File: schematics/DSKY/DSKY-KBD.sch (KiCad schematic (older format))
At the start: 64 parts, among them SW1 SW_Push, SW10 SW_Push, SW11 SW_Push, SW12 SW_Push, SW13 SW_Push, SW14 SW_Push, SW15 SW_Push, SW16 SW_Push, SW17 SW_Push, SW18 SW_Push, SW19 SW_Push, SW2 SW_Push, SW3 SW_Push, SW4 SW_Push, SW5 SW_Push, SW6 SW_Push, SW7 SW_Push, SW8 SW_Push, SW9 SW_Push, U1 74LS273, U10 74LS20, U11 74LS20, U12 74LS20, U13 74LS02, U14 74LS27, U15 74LS27, U16 74LS74, U18 74LS00, U19 74LS04, U2 74LS244, U3 LM555, U36 74LS00, U4 74LS04, U47 74LS126, U5 74LS04, U6 74LS00, U7 74LS08, U8 74LS10, U9 74LS20

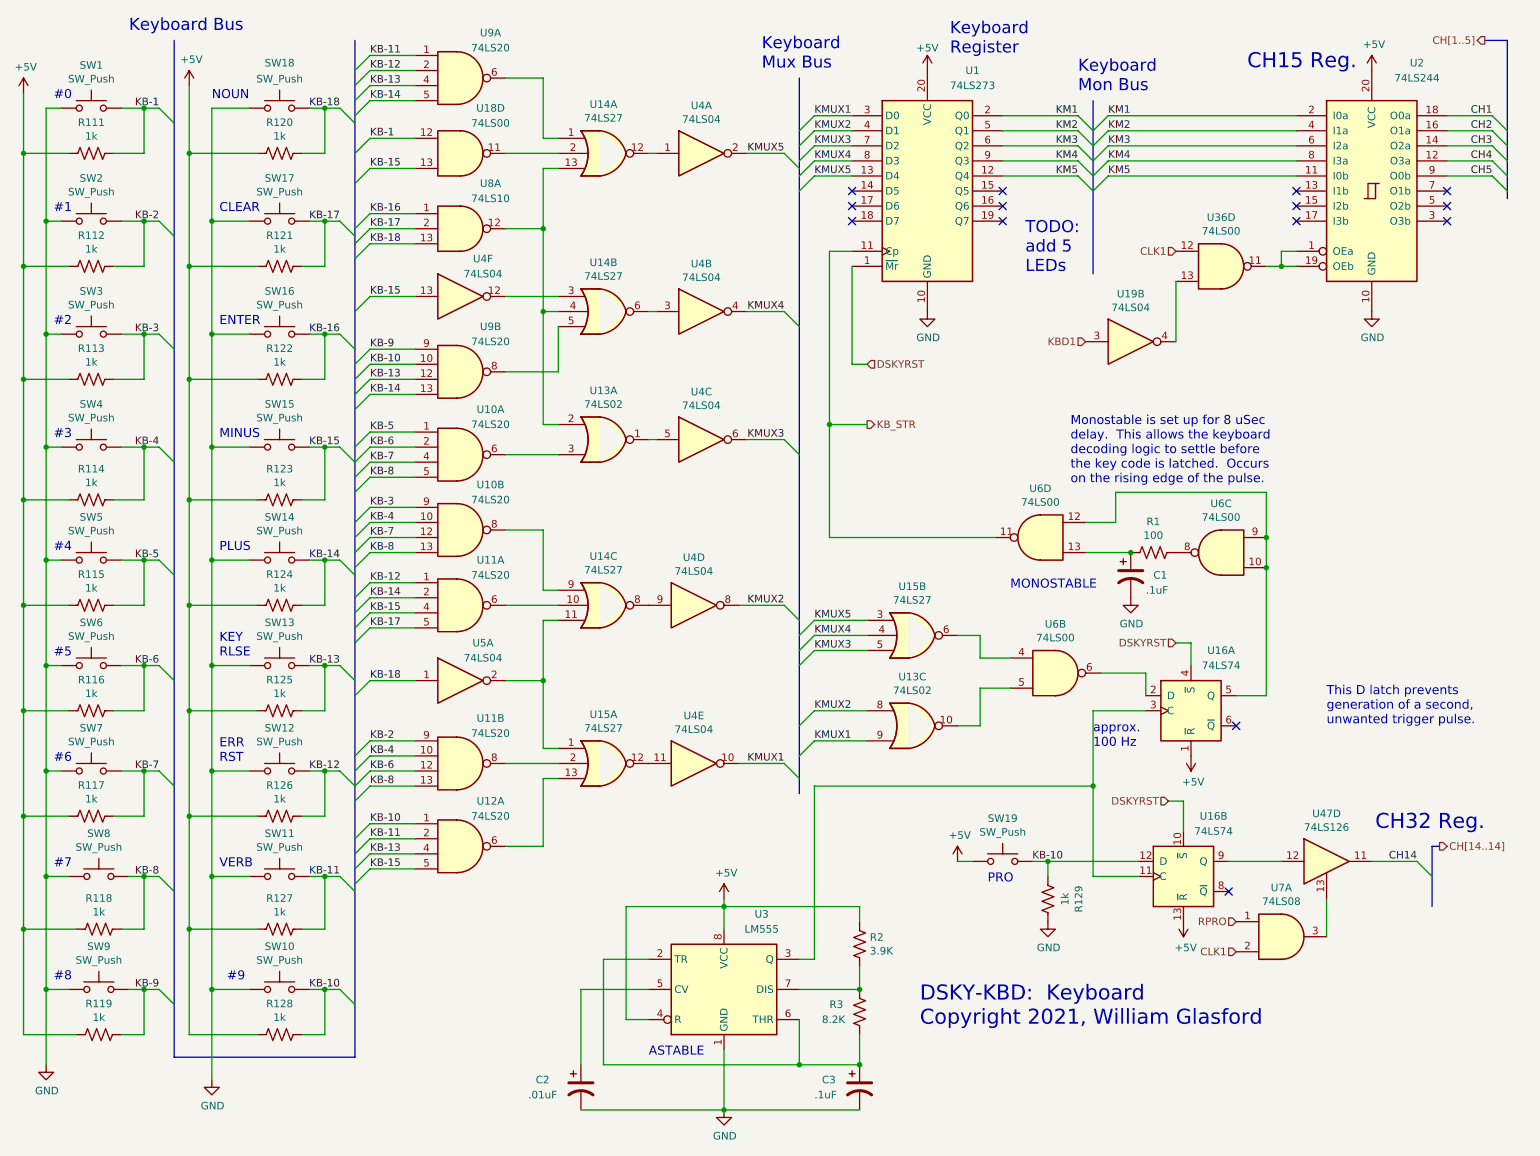
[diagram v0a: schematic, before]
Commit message: Using 4 LED driver chips.
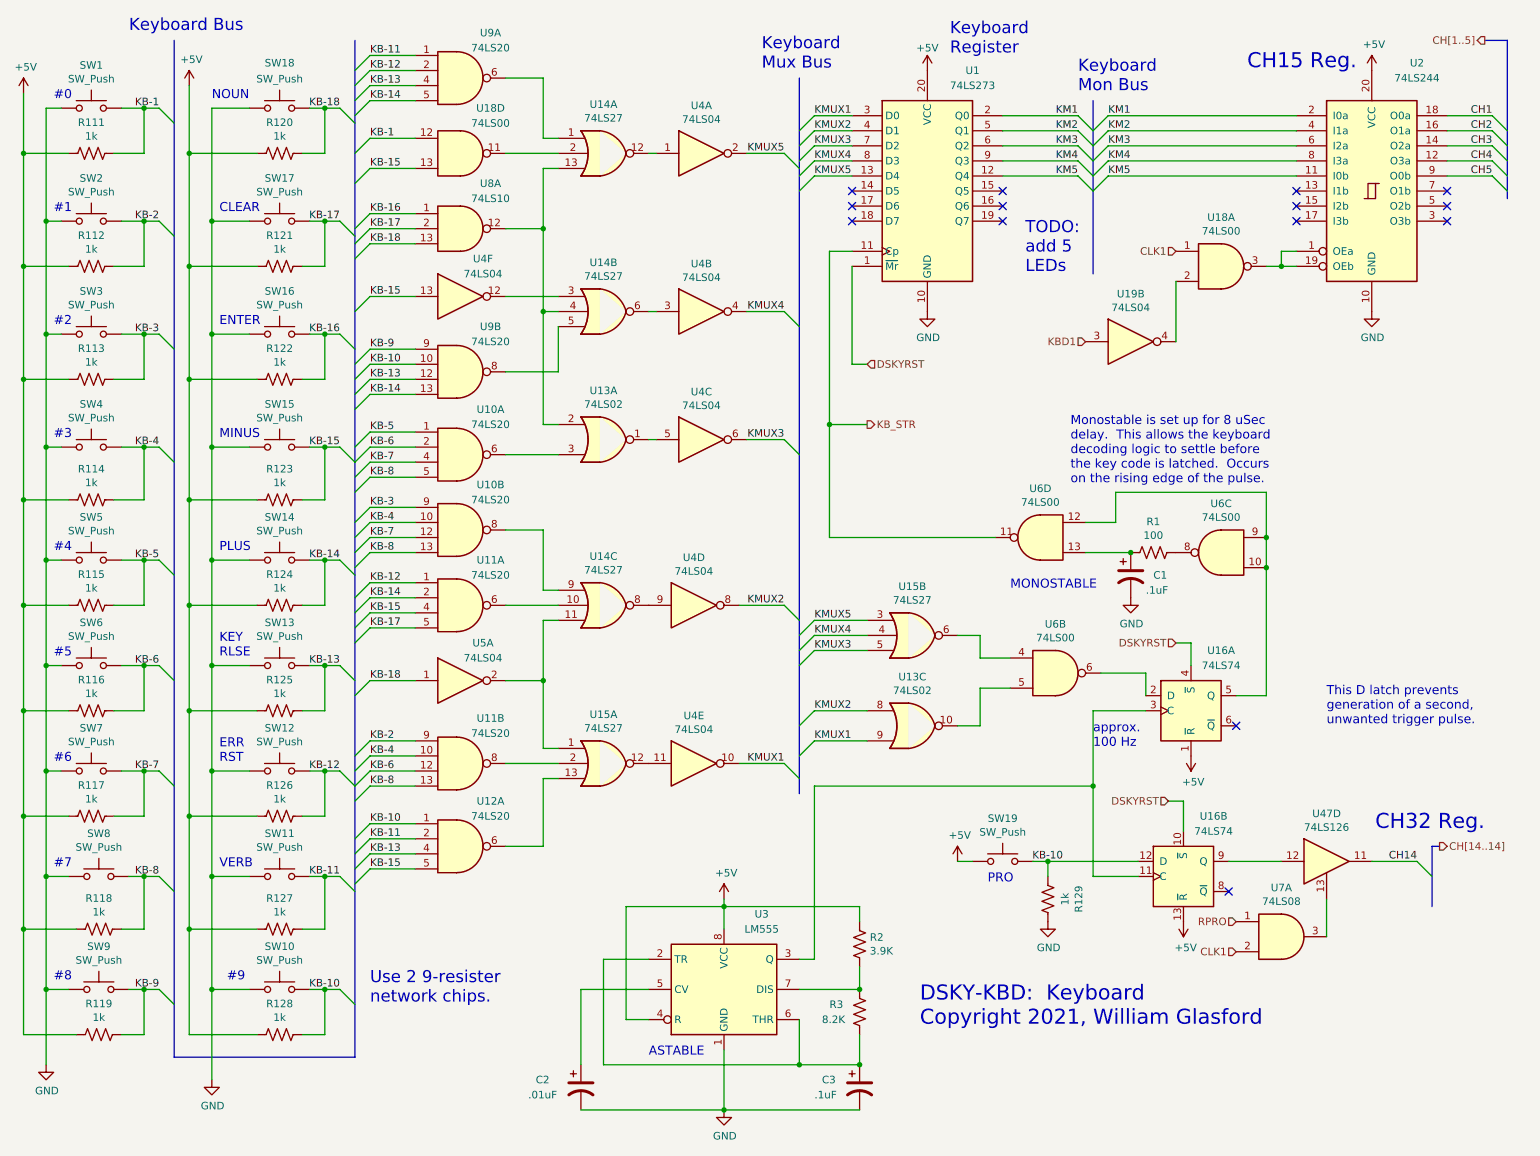
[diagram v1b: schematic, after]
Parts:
- renumbered U36 to U18
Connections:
- net CLK1: now also U18.1; no longer U18.12
- net at U2.1 (OEa), U2.19 (OEb): now also U18.3; no longer U18.11
- net at U19.4: now also U18.2; no longer U18.13
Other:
- note added: "Use 2 9-resister\nnetwork chips."
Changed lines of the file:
@@
 $Descr A 11000 8500
 encoding utf-8
-Sheet 3 15
+Sheet 13 13
 Title ""
 Date ""
@@
 Text Notes 6550 7200 0    100  ~ 0
 DSKY-KBD:  Keyboard\nCopyright 2021, William Glasford
+Text Notes 2900 7050 0    80   ~ 0
+Use 2 9-resister\nnetwork chips.
 Wire Wire Line
 	8300 5700 8200 5700
@@
 $EndComp
 $Comp
-L 74xx:74LS00 U36
-U 4 1 61A0A316
+L 74xx:74LS00 U18
+U 1 1 61A0A316
 P 8550 2150
-F 0 "U36" H 8550 2475 50  0000 C CNN
+F 0 "U18" H 8550 2475 50  0000 C CNN
 F 1 "74LS00" H 8550 2384 50  0000 C CNN
 F 2 "" H 8550 2150 50  0001 C CNN
 F 3 "http://www.ti.com/lit/gpn/sn74ls00" H 8550 2150 50  0001 C CNN
-	4    8550 2150
-	1    0    0    -1
-$EndComp
+	1    8550 2150
+	1    0    0    -1
+$EndComp
